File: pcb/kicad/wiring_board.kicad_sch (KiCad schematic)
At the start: 7 parts, among them J1 2604-1106, J2 5V out (flex jumper)

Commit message: Parts: replace the obsolete Murata capacitors, gold SSW socket on the EU 5 V board
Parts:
- C1: MPN GRM31CR61A226KE19L -> CL31A226KPHNNNE; Manufacturer Murata -> Samsung Electro-Mechanics
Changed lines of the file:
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@@
 			)
 		)
-		(property "Datasheet" "https://www.murata.com"
+		(property "Datasheet" "https://www.samsungsem.com"
 			(at 203.2 91.44 0)
 			(effects
@@
 			)
 		)
-		(property "Description" "Ceramic 22 uF 10 V X5R 1206 (or equivalent)"
+		(property "Description" "Ceramic 22 uF 10 V X5R 1206, 1.8 mm max (or equivalent)"
 			(at 203.2 91.44 0)
 			(effects
@@
 			)
 		)
-		(property "Manufacturer" "Murata"
+		(property "Manufacturer" "Samsung Electro-Mechanics"
 			(at 203.2 91.44 0)
 			(effects
@@
 			)
 		)
-		(property "MPN" "GRM31CR61A226KE19L"
+		(property "MPN" "CL31A226KPHNNNE"
 			(at 203.2 91.44 0)
 			(effects

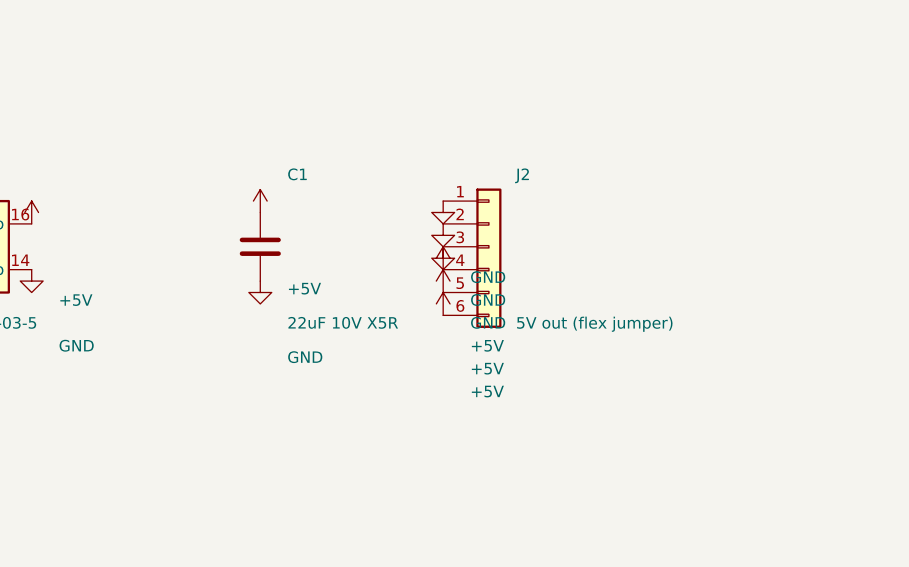
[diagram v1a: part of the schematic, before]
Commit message: Boards for v0.4: ring board, mic carrier, riser, cover flex, EU cap board, wiring board posts
- Ring board, mic carrier and riser in pcb/sensor/ (D-50, D-60, D-68); carrier and riser fab
  packs; the ring board waits on the MSR-2's CN2 part and map
- Riser 14 x 12 mm, pins above and between the posts; cover flex with the run past the GND
  contact post and a jog from the pad section (D-79)
- EU cap board on the carrier, closed snap windows, wider with the face plate (D-56, D-70,
  D-77, D-78); EU 5 V board pins follow the back cover's pads
- Wiring board: WA-SMSI spacer posts in the 5 V area (SMT, spigot inside the board), J2
- ERC / DRC clean on every board
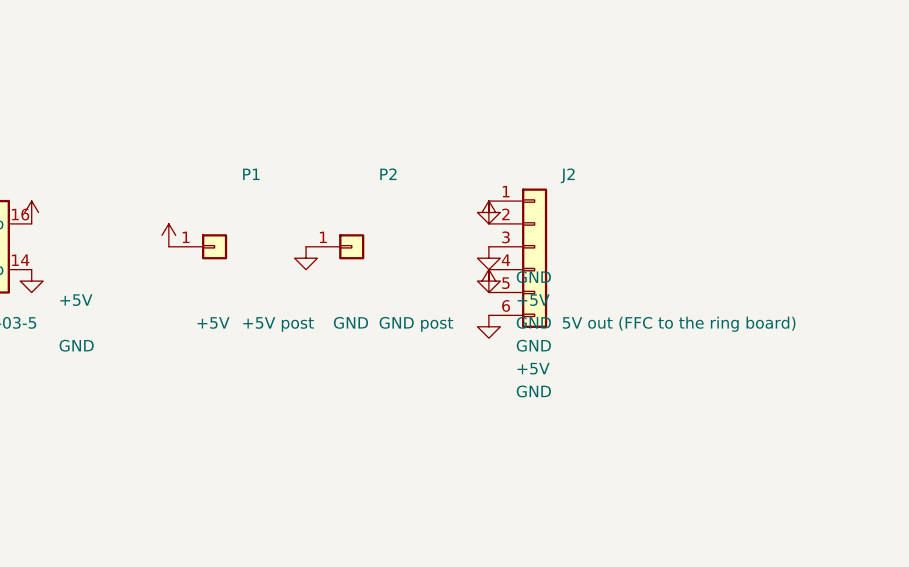
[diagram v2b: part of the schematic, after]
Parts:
- removed C1: 22uF 10V X5R, wiring_board:C_1206_3216Metric, symbol wiring_board:C
- added P1: +5V post, wiring_board:Wurth_WA-SMSI_M2_SMT_Spacer_L7mm, symbol wiring_board:Conn_01x01
- added P2: GND post, wiring_board:Wurth_WA-SMSI_M2_SMT_Spacer_L7mm, symbol wiring_board:Conn_01x01
- J2: value 5V out (flex jumper) -> 5V out (FFC to the ring board)
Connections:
- net +5V: now also J2.2 (Pin_2), P1.1 (Pin_1); no longer J2.4 (Pin_4), J2.6 (Pin_6)
- net GND: now also J2.4 (Pin_4), J2.6 (Pin_6), P2.1 (Pin_1); no longer J2.2 (Pin_2)
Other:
- moved on the sheet: J2

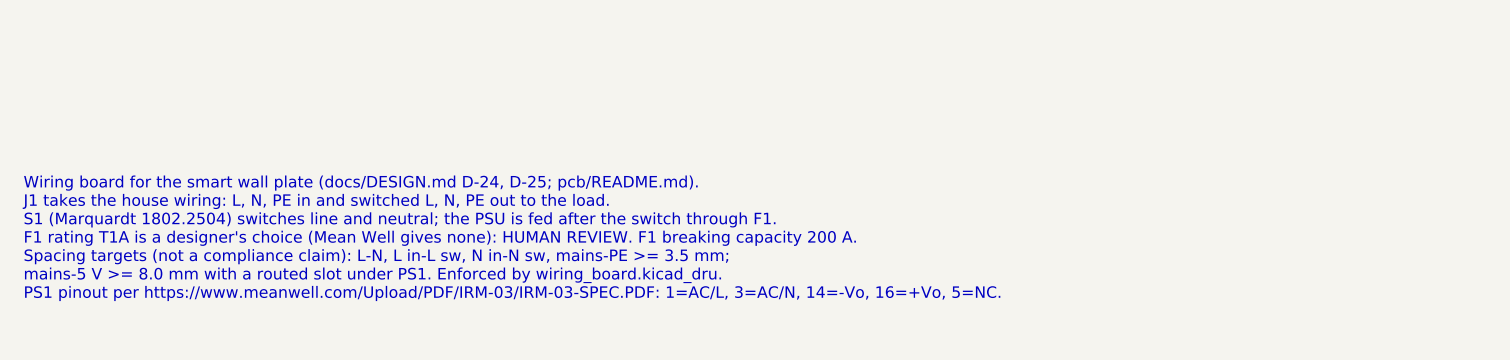
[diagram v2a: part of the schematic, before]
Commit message: Board generators: shared P70 and WA-SMSI footprints, fixed revision date, EU boards v0.4
- One Harwin P70 footprint with its 3D model for the riser and the EU 5 V board; one
  WA-SMSI land pattern for the wiring board posts and the ring board spacers
- Shared library-table and symbol helpers; dead code from removed boards gone
- REV_DATE replaces today's date on silkscreen and title blocks
- EU boards v0.4; EU cap board fab pack written once CN2 is confirmed
- Order lists key the EU header as TSM-102-02-L-SV (D-59)
- ERC / DRC clean on every board
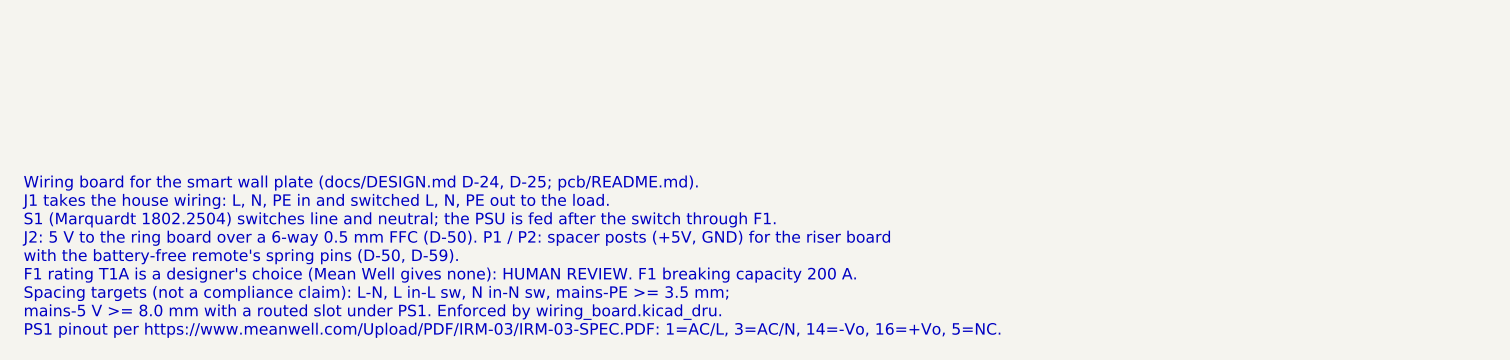
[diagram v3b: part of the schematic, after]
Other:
- note added: "Wiring board for the smart wall plate (docs/DESIGN.md D-24, D-25; pcb/README.md). J1 takes the house wiring: L, N, PE in and switched L, N, PE out to the load. S1 (Marquardt 1802.2504) switches line and neutral; the PSU is fed after the switch through F1. J2: 5 V to the ring board over a 6-way 0.5 mm FFC (D-50). P1 / P2: spacer posts (+5V, GND) for the riser board with the battery-free remote's s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"
- note removed: "Wiring board for the smart wall plate (docs/DESIGN.md D-24, D-25; pcb/README.md). J1 takes the house wiring: L, N, PE in and switched L, N, PE out to the load. S1 (Marquardt 1802.2504) switches line and neutral; the PSU is fed after the switch through F1. F1 rating T1A is a designer's choice (Mean Well gives none): HUMAN REVIEW. F1 breaking capacity 200 A. Spacing targets (not a compliance claim)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"
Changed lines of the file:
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@@
 		)
 	)
-	(text "Wiring board for the smart wall plate (docs/DESIGN.md D-24, D-25; pcb/README.md).\nJ1 takes the house wiring: L, N, PE in and switched L, N, PE out to the load.\nS1 (Marquardt 1802.2504) switches line and neutral; the PSU is fed after the switch through F1.\nF1 rating T1A is a designer's choice (Mean Well gives none): HUMAN REVIEW. F1 breaking capacity 200 A.\nSpacing targets (not a compliance claim): L-N, L in-L sw, N in-N sw, mains-PE >= 3.5 mm;\nmains-5 V >= 8.0 mm with a routed slot under PS1. Enforced by wiring_board.kicad_dru.\nPS1 pinout per https://www.meanwell.com/Upload/PDF/IRM-03/IRM-03-SPEC.PDF: 1=AC/L, 3=AC/N, 14=-Vo, 16=+Vo, 5=NC."
+	(text "Wiring board for the smart wall plate (docs/DESIGN.md D-24, D-25; pcb/README.md).\nJ1 takes the house wiring: L, N, PE in and switched L, N, PE out to the load.\nS1 (Marquardt 1802.2504) switches line and neutral; the PSU is fed after the switch through F1.\nJ2: 5 V to the ring board over a 6-way 0.5 mm FFC (D-50). P1 / P2: spacer posts (+5V, GND) for the riser board\nwith the battery-free remote's spring pins (D-50, D-59).\nF1 rating T1A is a designer's choice (Mean Well gives none): HUMAN REVIEW. F1 breaking capacity 200 A.\nSpacing targets (not a compliance claim): L-N, L in-L sw, N in-N sw, mains-PE >= 3.5 mm;\nmains-5 V >= 8.0 mm with a routed slot under PS1. Enforced by wiring_board.kicad_dru.\nPS1 pinout per https://www.meanwell.com/Upload/PDF/IRM-03/IRM-03-SPEC.PDF: 1=AC/L, 3=AC/N, 14=-Vo, 16=+Vo, 5=NC."
 		(exclude_from_sim no)
 		(at 25 125 0)

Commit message: Mic on the boards, parts audit, rocker second source, CN2 land pattern, back cover fit (D-82..D-90)
- Prototype PCBWay packs for the ring board, EU cap board and cover flex; logos and URL on the
  boards with room for them
- CN2 mate: Molex 55909-2474 on an assumed 51338-2474 (D-82); land pattern from Molex
  SD-55909-003 rev J, B2B from SD-51338-003 rev K (D-89); contact map and pin 1 still open
- Microphone: Knowles SPK0641HT4H-1 + ADAU7002 on the ring board and the EU cap board, the mic
  carrier removed; face plate sound column on a gasket (D-83); C3 KEMET C1206C104J3GACTU C0G
  (D-85)
- Parts rule (active, stocked at DigiKey or Mouser) and audit: F1 3403.0166.11, cover flex 1 uF
  CL05A105KO5NNNC, rocker at Mouser 979-1802.2504 (D-84)
- Rocker: tabs soldered into plated slots accepted (D-86); E-Switch RA412C1100 second source,
  slotted footprint on the wiring board and the EU mains board, solder the rocker after the
  board is screwed down (D-88)
- Back cover: round-over 8.1 x 8.0 from the printed gauges (D-87); four tabs inside the long
  side walls into the housing's slots (D-90); back_gauges_PLA
- make stock / make order-push (pcb/tools/distributors.py): live DigiKey / Mouser stock and
  lifecycle, DigiKey myLists link and Mouser cart; keys from the environment only
- Boards ERC / DRC clean; make check, make eu, make check-renders pass; renders, fab and
  order packs regenerated
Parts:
- F1: MPN 3404.2416.22 -> 3403.0166.11
- S1: footprint wiring_board:Marquardt_1802.2504_DPST_PCB -> wiring_board:Rocker_DPST_Marquardt_1802.2504_E-Switch_RA412C1100
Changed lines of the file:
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@@
 			)
 		)
-		(property "Footprint" "wiring_board:Marquardt_1802.2504_DPST_PCB"
+		(property "Footprint" "wiring_board:Rocker_DPST_Marquardt_1802.2504_E-Switch_RA412C1100"
 			(at 76.2 91.44 0)
 			(effects
@@
 			)
 		)
-		(property "MPN" "3404.2416.22"
+		(property "MPN" "3403.0166.11"
 			(at 111.76 91.44 0)
 			(effects

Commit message: Flex review fixes, back cover clip, README, Sladdseg, order lists (D-116..D-119)
- D-116: cover flex: 0603 X5R input/output caps, ESD diode TPD1E10B06DYAR,
  0.6 mm bend radius with relief slits, stiffener notch and outlines,
  coverlay expansion, mask-defined pin pads, teardrops, fab notes; the
  cover's snap hooks allow for stiffener adhesive and tolerance
- D-117, D-118: bottom clip catch 3.22 above the floor, tip as far proud of
  the shell as the top clip's
- Battery polarity confirmed on a unit
- README rewritten: three editions, assembly renders, safety and polarity
  warnings, cost for 1 to 10,000 plates, printed parts; detail and board
  renders moved to their docs; the product is named Sladdseg
- EU boards: the ant logo on the other face
- D-119: order lists: one NA plate, one EU plate, a devkit of 5 + 5
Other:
- title: Smart wall plate - wiring board -> Sladdseg - wiring board
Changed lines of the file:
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@@
 	(paper "A4")
 	(title_block
-		(title "Smart wall plate - wiring board")
+		(title "Sladdseg - wiring board")
 		(date "2026-10-12")
 		(rev "v0.5")
